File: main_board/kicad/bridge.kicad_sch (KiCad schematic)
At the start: 21 parts, among them Q13 IRFB3077, Q14 IRFB3077, Q15 IRFB3077, Q16 IRFB3077, Q17 IRFB3077, Q18 IRFB3077

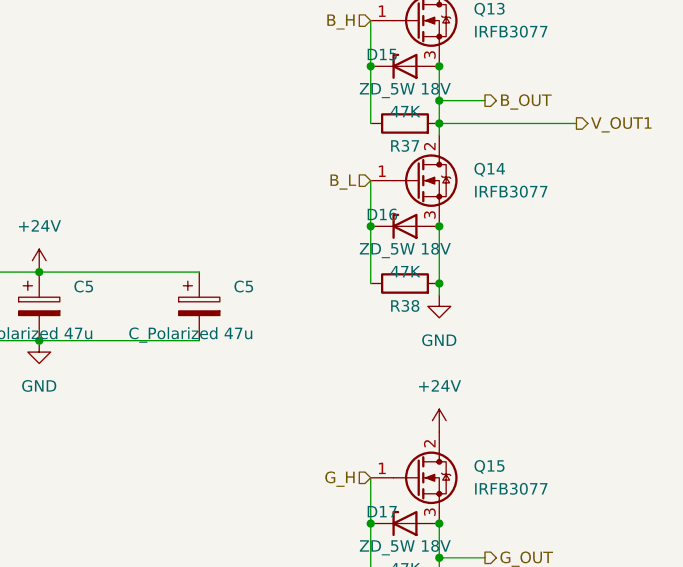
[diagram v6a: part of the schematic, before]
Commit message: implemented bridge and first bridge driver as well as both step converters on the pcd layout
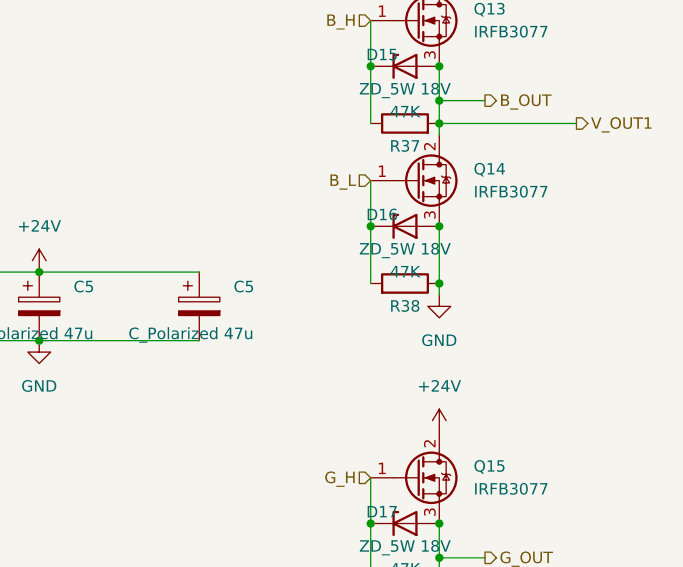
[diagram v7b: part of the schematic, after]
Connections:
- net B_L: now also R38.2; no longer R38.1
- net GND: now also R38.1; no longer R38.2
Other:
- moved on the sheet: R38
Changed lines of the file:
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@@
     )
   )
-  (symbol (lib_id "Device:R") (at 113.03 64.77 90) (unit 1)
+  (symbol (lib_id "Device:R") (at 113.03 64.77 270) (mirror x) (unit 1)
     (in_bom yes) (on_board yes) (dnp no)
     (property "Reference" "R38" (at 113.03 67.31 90)
